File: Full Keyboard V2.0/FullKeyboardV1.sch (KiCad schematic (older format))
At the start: 203 parts, among them SW1 Esc, SW10 2, SW11 W, SW12 S, SW13 Z, SW15 3, SW16 E, SW17 D, SW18 X, SW19 4, SW2 Tab, SW20 R, SW21 F, SW22 C, SW23 5, SW24 T, SW25 G, SW26 V, SW27 6, SW28 Y, SW29 H, SW3 Caps, SW30 B, SW32 7, SW33 U, SW34 J, SW35 N, SW36 8, SW37 I, SW38 K, SW39 M, SW4 LShift, SW40 9, SW41 O, SW42 L, SW43 <, SW44 0, SW45 P, SW46 ;, SW47 >, SW49 Minus, SW5 End/Home, SW50 [, SW51 \", SW52 /, SW54 =, SW55 ], SW56 Up, SW57 RShift, SW59 BKSPC, SW6 1, SW60 \\, SW61 Enter, SW63 Til, SW64 Del, SW65 Pg Up, SW66 Pg Dw, SW7 Q, SW8 A, U5 Cherry_bottom_row

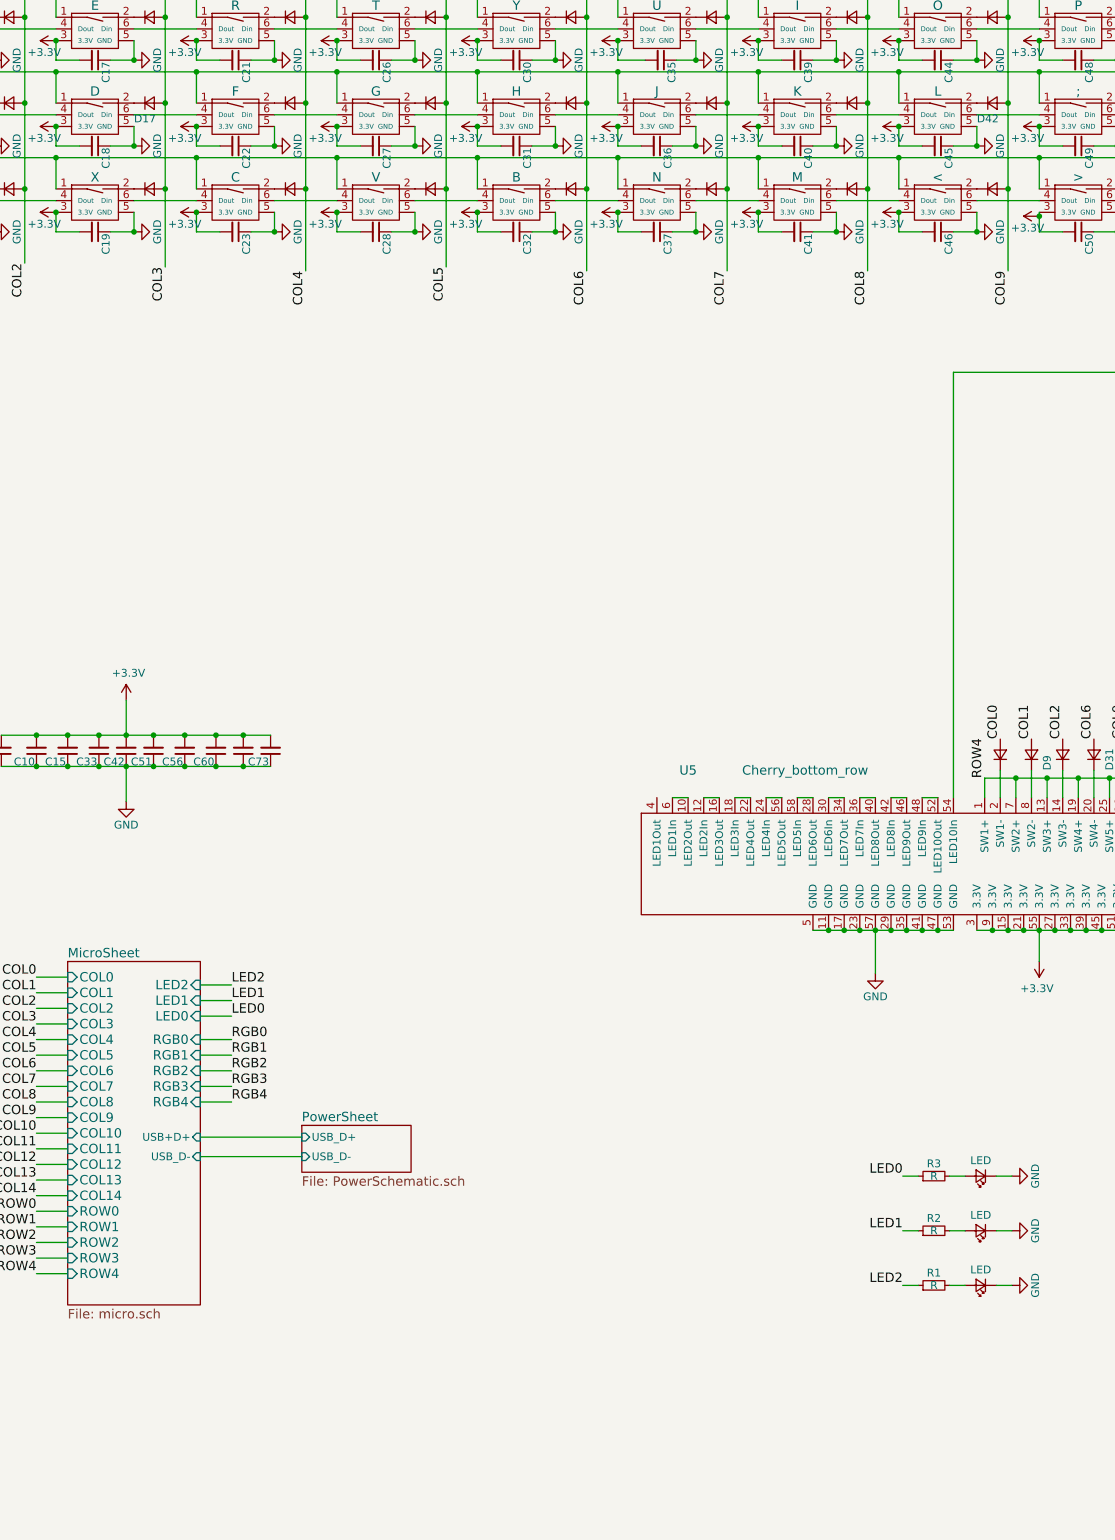
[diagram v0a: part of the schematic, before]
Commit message: Added USB HUB
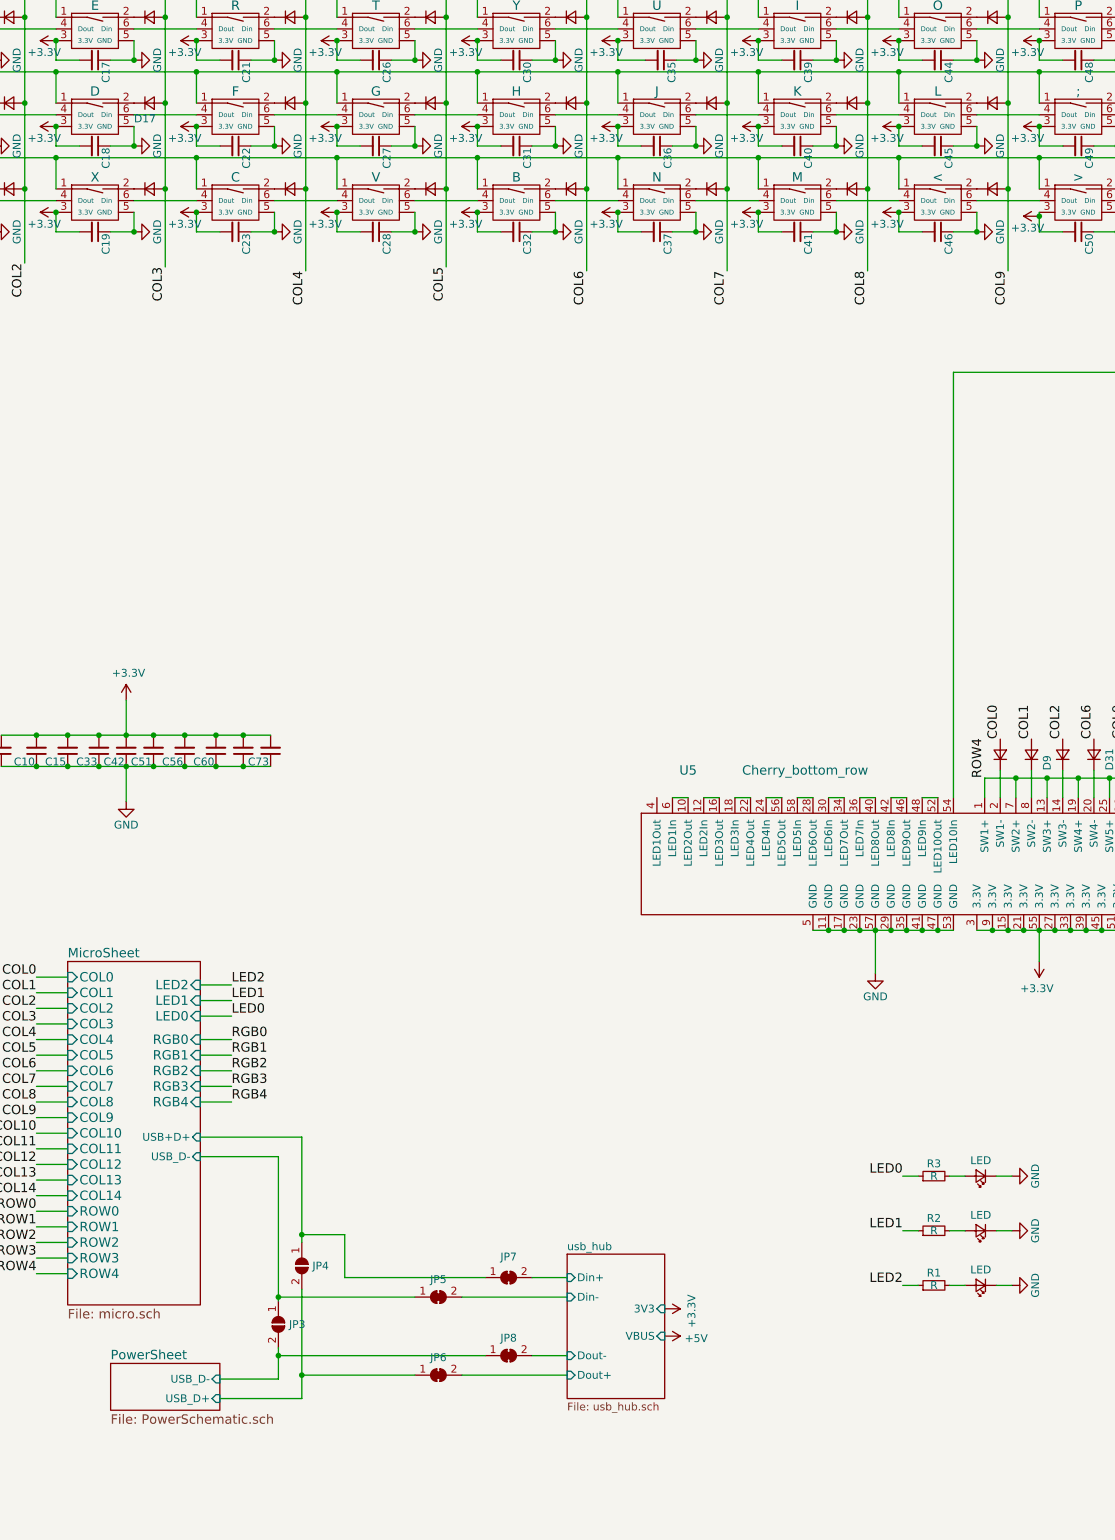
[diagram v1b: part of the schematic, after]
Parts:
- added JP3, JP4: SolderJumper_2_Open, Jumper:SolderJumper-2_P1.3mm_Open_RoundedPad1.0x1.5mm, symbol Jumper:SolderJumper_2_Open
- added JP5, JP6, JP7, JP8: SolderJumper_2_Bridged, Jumper:SolderJumper-2_P1.3mm_Bridged_RoundedPad1.0x1.5mm, symbol Jumper:SolderJumper_2_Bridged
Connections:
- net MicroSheet/USB+D+: now also JP4.1 (A), JP7.1 (A)
- net MicroSheet/USB_D-: now also JP3.1 (A), JP5.1 (A)
- new net PowerSheet/USB_D+: JP4.2 (B), JP6.1 (A)
- new net PowerSheet/USB_D-: JP3.2 (B), JP8.1 (A)
- new net usb_hub/Din+: JP7.2 (B)
- new net usb_hub/Din-: JP5.2 (B)
- new net usb_hub/Dout+: JP6.2 (B)
- new net usb_hub/Dout-: JP8.2 (B)
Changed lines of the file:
@@
 $Descr A4 11693 8268
 encoding utf-8
-Sheet 1 3
+Sheet 1 4
 Title ""
 Date ""
@@
 Text Label 2475 5050 2    60   ~ 0
 ROW4
-$Sheet
-S 4175 4100 700  300
-U 586925EB
-F0 "PowerSheet" 60
-F1 "PowerSchematic.sch" 60
-F2 "USB_D-" I L 4175 4300 50
-F3 "USB_D+" I L 4175 4175 50
-$EndSheet
 $Comp
 L keyboard:LED_SWITCH SW1
@@
 U 1 1 59B874AB
 P 8600 -2450
-F 0 "D42" H 8500 -2550 50  00000100 L CNN
+F 0 "D42" H 8500 -2550 50  0001 L CNN
 F 1 "D_Small" H 8450 -2530 50  0001 L CNN
 F 2 "Diode_SMD:D_SOD-123" V 8600 -2450 50  0001 C CNN
@@
 F31 "USB+D+" I R 3525 4175 50
 $EndSheet
-Wire Wire Line
-	3525 4175 4175 4175
-Wire Wire Line
-	4175 4300 3525 4300
 Connection ~ 8900 2850
 Connection ~ 7850 2850
@@
 	-1   0    0    1
 $EndComp
+$Sheet
+S 5875 4925 625  925
+U 5E9ACD38
+F0 "usb_hub" 50
+F1 "usb_hub.sch" 50
+F2 "Dout+" I L 5875 5700 50
+F3 "Dout-" I L 5875 5575 50
+F4 "Din+" I L 5875 5075 50
+F5 "Din-" I L 5875 5200 50
+F6 "VBUS" I R 6500 5450 50
+F7 "3V3" I R 6500 5275 50
+$EndSheet
+$Comp
+L power:+5V #PWR0153
+U 1 1 5EA5A8A9
+P 6500 5450
+F 0 "#PWR0153" H 6500 5300 50  0001 C CNN
+F 1 "+5V" V 6515 5578 50  0000 L CNN
+F 2 "" H 6500 5450 50  0001 C CNN
+F 3 "" H 6500 5450 50  0001 C CNN
+	1    6500 5450
+	0    1    1    0
+$EndComp
+$Comp
+L FullKeyboardV1-cache:+3.3V #PWR0154
+U 1 1 5EA5BADF
+P 6500 5275
+F 0 "#PWR0154" H 6500 5125 50  0001 C CNN
+F 1 "+3.3V" H 6515 5448 50  0000 C CNN
+F 2 "" H 6500 5275 50  0001 C CNN
+F 3 "" H 6500 5275 50  0001 C CNN
+	1    6500 5275
+	0    1    1    0
+$EndComp
+Wire Wire Line
+	4025 5725 4025 5575
+$Comp
+L Jumper:SolderJumper_2_Bridged JP7
+U 1 1 5ED36A74
+P 5500 5075
+F 0 "JP7" H 5500 4942 50  0000 C CNN
+F 1 "SolderJumper_2_Bridged" H 5500 4941 50  0001 C CNN
+F 2 "Jumper:SolderJumper-2_P1.3mm_Bridged_RoundedPad1.0x1.5mm" H 5500 5075 50  0001 C CNN
+F 3 "~" H 5500 5075 50  0001 C CNN
+	1    5500 5075
+	1    0    0    1
+$EndComp
+$Comp
+L Jumper:SolderJumper_2_Bridged JP5
+U 1 1 5ED36DFE
+P 5050 5200
+F 0 "JP5" H 5050 5313 50  0000 C CNN
+F 1 "SolderJumper_2_Bridged" H 5050 5314 50  0001 C CNN
+F 2 "Jumper:SolderJumper-2_P1.3mm_Bridged_RoundedPad1.0x1.5mm" H 5050 5200 50  0001 C CNN
+F 3 "~" H 5050 5200 50  0001 C CNN
+	1    5050 5200
+	1    0    0    -1
+$EndComp
+$Comp
+L Jumper:SolderJumper_2_Bridged JP8
+U 1 1 5ED372C9
+P 5500 5575
+F 0 "JP8" H 5500 5688 50  0000 C CNN
+F 1 "SolderJumper_2_Bridged" H 5500 5689 50  0001 C CNN
+F 2 "Jumper:SolderJumper-2_P1.3mm_Bridged_RoundedPad1.0x1.5mm" H 5500 5575 50  0001 C CNN
+F 3 "~" H 5500 5575 50  0001 C CNN
+	1    5500 5575
+	1    0    0    -1
+$EndComp
+$Comp
+L Jumper:SolderJumper_2_Bridged JP6
+U 1 1 5ED376F0
+P 5050 5700
+F 0 "JP6" H 5050 5813 50  0000 C CNN
+F 1 "SolderJumper_2_Bridged" H 5050 5814 50  0001 C CNN
+F 2 "Jumper:SolderJumper-2_P1.3mm_Bridged_RoundedPad1.0x1.5mm" H 5050 5700 50  0001 C CNN
+F 3 "~" H 5050 5700 50  0001 C CNN
+	1    5050 5700
+	1    0    0    -1
+$EndComp
+$Comp
+L Jumper:SolderJumper_2_Open JP3
+U 1 1 5ED38136
+P 4025 5375
+F 0 "JP3" V 4025 5443 50  0000 L CNN
+F 1 "SolderJumper_2_Open" V 4070 5443 50  0001 L CNN
+F 2 "Jumper:SolderJumper-2_P1.3mm_Open_RoundedPad1.0x1.5mm" H 4025 5375 50  0001 C CNN
+F 3 "~" H 4025 5375 50  0001 C CNN
+	1    4025 5375
+	0    1    1    0
+$EndComp
+$Comp
+L Jumper:SolderJumper_2_Open JP4
+U 1 1 5ED38895
+P 4175 5000
+F 0 "JP4" V 4175 5068 50  0000 L CNN
+F 1 "SolderJumper_2_Open" V 4220 5068 50  0001 L CNN
+F 2 "Jumper:SolderJumper-2_P1.3mm_Open_RoundedPad1.0x1.5mm" H 4175 5000 50  0001 C CNN
+F 3 "~" H 4175 5000 50  0001 C CNN
+	1    4175 5000
+	0    1    1    0
+$EndComp
+Wire Wire Line
+	4175 4175 4175 4800
+Wire Wire Line
+	3525 4175 4175 4175
+Wire Wire Line
+	3525 4300 4025 4300
+Wire Wire Line
+	4175 4800 4450 4800
+Wire Wire Line
+	4450 4800 4450 5075
+Wire Wire Line
+	4450 5075 5350 5075
+Connection ~ 4175 4800
+Wire Wire Line
+	4175 4800 4175 4850
+Wire Wire Line
+	4025 4300 4025 5200
+Wire Wire Line
+	4900 5200 4025 5200
+Connection ~ 4025 5200
+Wire Wire Line
+	4025 5200 4025 5225
+Wire Wire Line
+	4175 5150 4175 5700
+Wire Wire Line
+	3650 5850 4175 5850
+Wire Wire Line
+	5875 5075 5650 5075
+Wire Wire Line
+	5200 5200 5875 5200
+Wire Wire Line
+	5650 5575 5875 5575
+Wire Wire Line
+	5875 5700 5200 5700
+Wire Wire Line
+	5350 5575 4025 5575
+Wire Wire Line
+	4025 5575 4025 5525
+Connection ~ 4025 5575
+Wire Wire Line
+	4900 5700 4175 5700
+Connection ~ 4175 5700
+Wire Wire Line
+	4175 5700 4175 5850
+$Sheet
+S 2950 5625 700  300
+U 586925EB
+F0 "PowerSheet" 60
+F1 "PowerSchematic.sch" 60
+F2 "USB_D-" I R 3650 5725 50
+F3 "USB_D+" I R 3650 5850 50
+$EndSheet
+Wire Wire Line
+	4025 5725 3650 5725
 $EndSCHEMATC

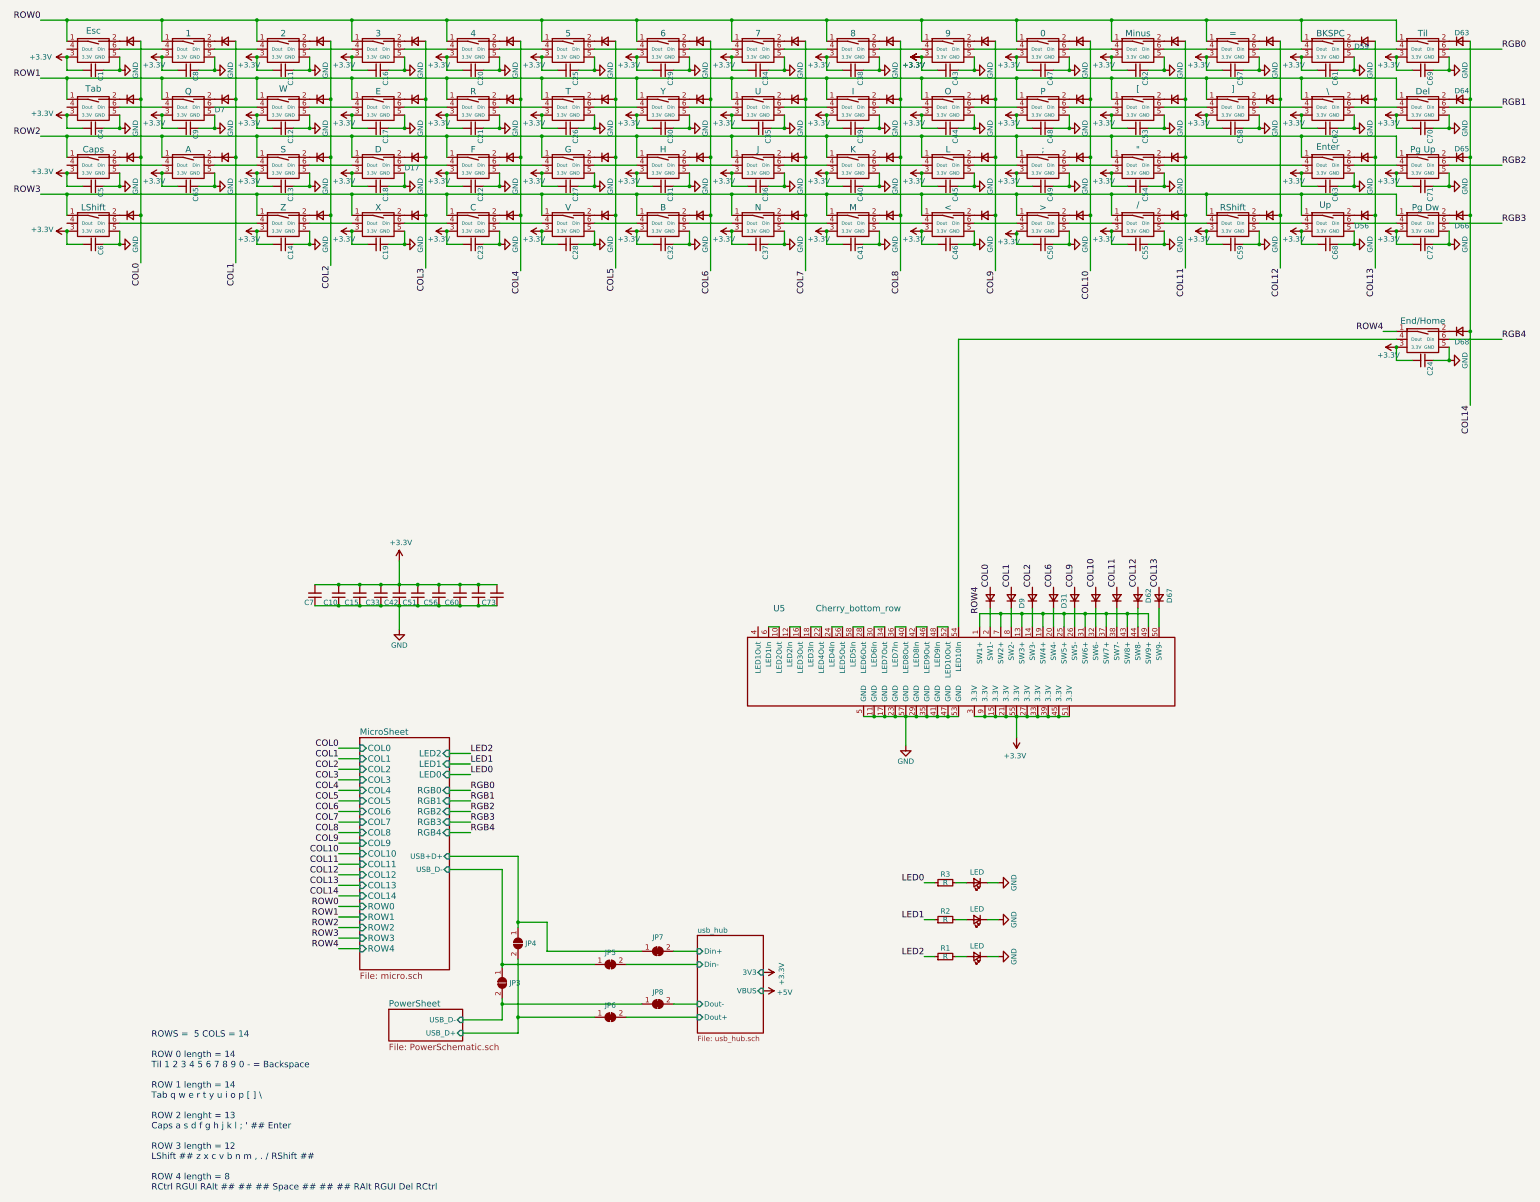
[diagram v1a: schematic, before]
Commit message: Added multi-function left and right shift
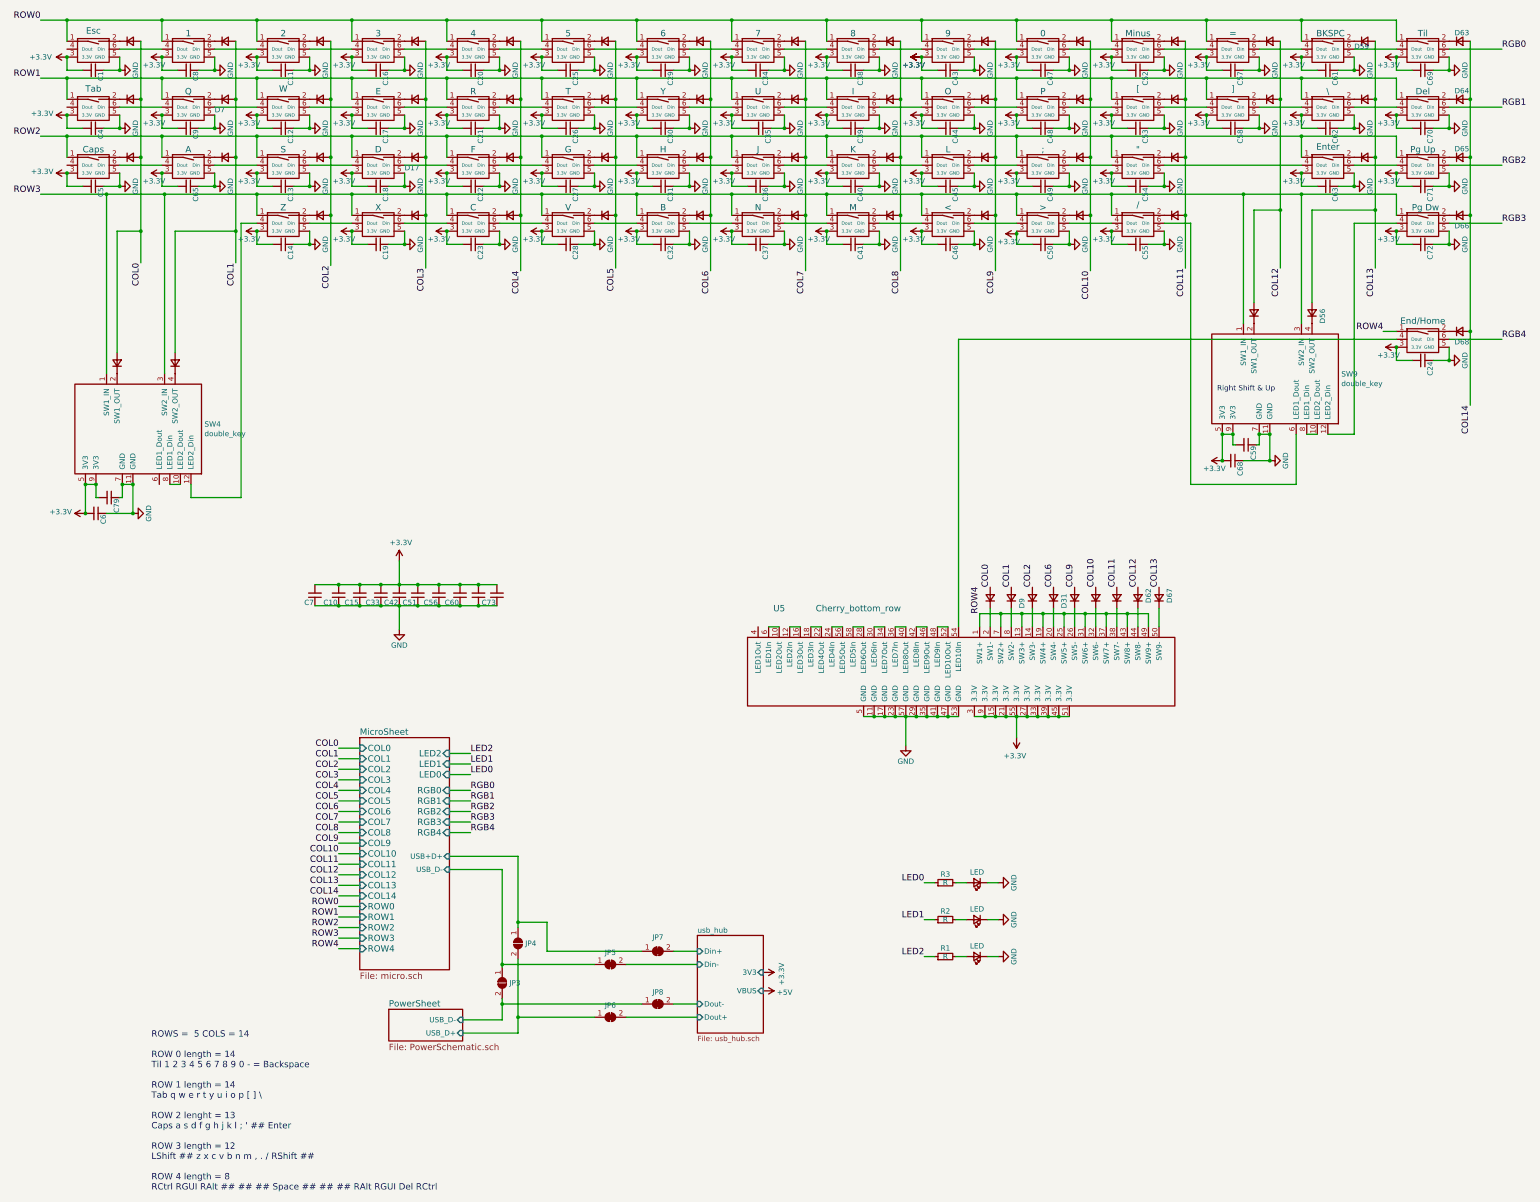
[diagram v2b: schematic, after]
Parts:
- removed SW4: LShift, keyboard:RGB_CHERRY_PCB_200H, symbol keyboard:LED_SWITCH
- removed SW56: Up, keyboard:RGB_CHERRY_PCB_100H, symbol keyboard:LED_SWITCH
- removed SW57: RShift, keyboard:RGB_CHERRY_PCB_175H, symbol keyboard:LED_SWITCH
- added C79: C_Small, Capacitor_SMD:C_0603_1608Metric, symbol Device:C_Small
- added D77: D_Small, Diode_SMD:D_SOD-123, symbol Device:D_Small
- added SW4: double_key, keyboard:RGB_CHERRY_SHIFT_ROW_LEFT, symbol keyboard:double_key
- added SW9: double_key, keyboard:RGB_CHERRY_SHIFT_RIGHT_2.0, symbol keyboard:double_key
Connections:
- net +3V3: now also C79.2, SW4.5 (3V3), SW4.9 (3V3), SW9.5 (3V3), SW9.9 (3V3)
- net COL1: now also D77.2 (A)
- net GND: now also C79.1, SW4.11 (GND), SW4.7 (GND), SW9.11 (GND), SW9.7 (GND)
- net ROW3: now also SW4.1 (SW1_IN), SW4.3 (SW2_IN), SW9.1 (SW1_IN), SW9.3 (SW2_IN)
- net at D4.1 (K): now also SW4.2 (SW1_OUT)
- net at SW13.4 (Dout): now also SW4.12 (LED2_Din)
- net at SW52.6 (Din): now also SW9.6 (LED1_Dout)
- net at D56.1 (K): now also SW9.4 (SW2_OUT)
- net at SW66.4 (Dout): now also SW9.12 (LED2_Din)
- net at D57.1 (K): now also SW9.2 (SW1_OUT)
- new net: SW9.10 (LED2_Dout), SW9.8 (LED1_Din)
- new net: D77.1 (K), SW4.4 (SW2_OUT)
- new net: SW4.10 (LED2_Dout), SW4.8 (LED1_Din)
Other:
- note added: "Right Shift & Up"
- moved on the sheet: C59, C6, C68, D56
